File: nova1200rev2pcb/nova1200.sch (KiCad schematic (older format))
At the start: 190 parts, among them J1 Conn_02x26_Odd_Even, J2 Conn_02x05_Top_Bottom, J3 Conn_02x05_Top_Bottom, J4 Conn_02x01, J5 Conn_02x09_Odd_Even, J6 Conn_01x09, SW1 SW_SPST, SW10 SW_SPST, SW11 SW_SPST, SW12 SW_SPST, SW13 SW_SPST, SW14 SW_SPST, SW15 SW_SPST, SW16 SW_SPST, SW17 SW_SPDT_MSM, SW18 SW_SPDT_MSM, SW19 SW_SPDT_MSM, SW2 SW_SPST, SW20 SW_SPDT_MSM, SW21 SW_SPDT_MSM, SW22 SW_SPDT_MSM, SW23 SW_SPDT_MSM, SW24 SW_SPDT_MSM, SW25 SW_SPDT_MSM, SW26 SW_SPDT_MSM, SW3 SW_SPST, SW4 SW_SPST, SW5 SW_SPST, SW6 SW_SPST, SW7 SW_SPST, SW8 SW_SPST, SW9 SW_SPST, U1 74LS257, U10 74LS173, U11 74LS173, U12 74LS173, U13 74LS173, U14 74LS173, U15 74LS257, U16 74LS42, U17 74LS42, U18 74LS02, U19 74LS06, U2 74LS257, U20 74LS06, U21 74LS06, U3 74LS257, U4 74LS257, U5 74LS173, U6 74LS173, U7 74LS173, U8 74LS173, U9 74LS173

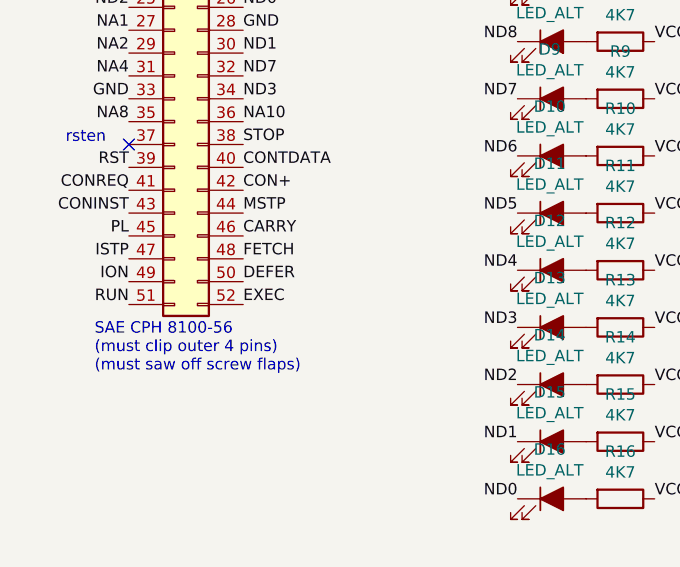
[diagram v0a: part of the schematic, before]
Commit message: Fixed error in pcb where EXEC and DEFER where swapped
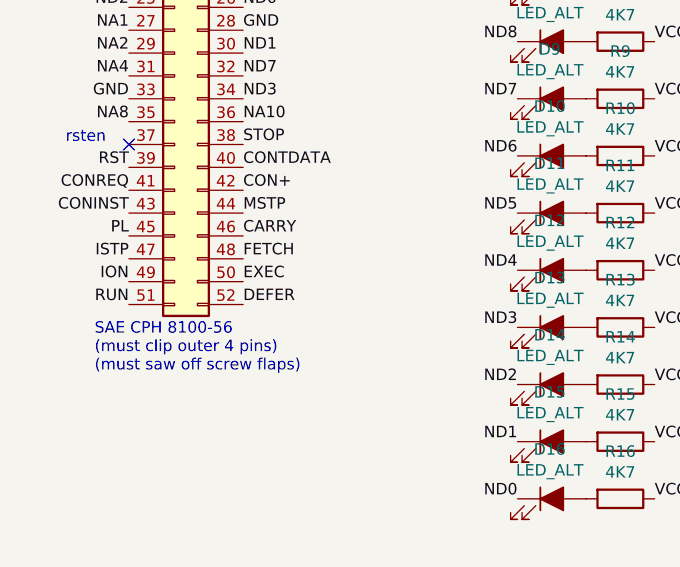
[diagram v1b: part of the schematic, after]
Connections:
- net DEFER: now also J1.52 (Pin_52); no longer J1.50 (Pin_50)
- net EXEC: now also J1.50 (Pin_50); no longer J1.52 (Pin_52)
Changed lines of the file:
@@
 Comment2 "Add pinheader for control switches"
 Comment3 "Idea: add extra register on SEL7"
-Comment4 ""
+Comment4 "Swapped EXEC and DEFER"
 $EndDescr
 $Comp
@@
 FETCH
 Text Label 1450 8900 0    50   ~ 0
+EXEC
+Text Label 1450 9000 0    50   ~ 0
 DEFER
-Text Label 1450 9000 0    50   ~ 0
-EXEC
 Text Notes 1500 7100 0    50   ~ 0
 vlamp

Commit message: Added jumper/resistor for Teensy application
// Nano to Teensy mapping:
//Arduino Teensy 3.5 Application
//GND	GND	GND
//D2	D0	D0
//..	..	..
//D12	D10	ENLCD1
//D13	A1	ENLCD2
//A0	A4	--- (KEYP)
//A1	A5	---
//A2	A6	LCD4
//A3	A7	LCD5
//A4	A8	LCD6
//A5	A9	LCD7
//A6	X (3.3 V)	---
//A7	--- (AGND)	---
//5V	Vin	5V
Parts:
- added R69: Jumper, Resistor_THT:R_Axial_DIN0204_L3.6mm_D1.6mm_P5.08mm_Horizontal, symbol Device:R_Small
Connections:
- net KEYL: now also R69.2
- net KEYP: now also R69.1
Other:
- note added: "A0"
- note added: "A0'"
- note added: "A1"
- note added: "A2"
- note added: "ENLCD1"
- note added: "ENLCD2"
- note added: "ERRORS: PINHEADERS WRONG FOOTPRINT\nAREF NOT CONNECTED TO KEYCHAIN; \nHole size Nova conn"
- note added: "FREE"
- note added: "I2C"
- note added: "I2C. LCD7"
- note added: "LCD4"
- note added: "LCD5"
- note added: "LCD6"
- note added: "Place when using Teensy 3.5 processor"
- note added: "Proposed to allow SPI"
- note added: "Proposed to isolate I2C \nfrom LCD"
- note added: "SPI"
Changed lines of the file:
@@
 Sheet 1 1
 Title "Computer controlled front panel for Nova 1200 computer"
-Date "2019-01-01"
+Date "2019-03-02"
 Rev "2"
 Comp "Marcel van Herk"
@@
 Comment2 "Add pinheader for control switches"
 Comment3 "Idea: add extra register on SEL7"
-Comment4 "Swapped EXEC and DEFER"
+Comment4 "Swapped EXEC and DEFER; added Teensy jumper"
 $EndDescr
 $Comp
@@
 Connection ~ 14800 8550
 Wire Wire Line
-	14400 8500 14600 8500
+	14400 8500 14450 8500
 Connection ~ 14600 8500
 Wire Wire Line
@@
 GND
 NoConn ~ 7650 7250
+Text Notes 12300 7100 0    50   ~ 0
+SPI
+Text Notes 12300 7200 0    50   ~ 0
+SPI
+Text Notes 12300 7300 0    50   ~ 0
+SPI
+Text Notes 12500 7000 0    50   ~ 0
+A0
+Text Notes 12500 7100 0    50   ~ 0
+A1
+Text Notes 12500 7200 0    50   ~ 0
+A2
+Text Notes 12500 7300 0    50   ~ 0
+A0'
+Text Notes 12450 6600 0    50   ~ 0
+ENLCD1
+Text Notes 12450 6700 0    50   ~ 0
+ENLCD2
+Text Notes 11800 6450 0    50   ~ 0
+Proposed to allow SPI
+Text Notes 14200 6700 0    50   ~ 0
+LCD4
+Text Notes 14200 6800 0    50   ~ 0
+LCD5
+Text Notes 14200 6900 0    50   ~ 0
+LCD6
+Text Notes 14200 7000 0    50   ~ 0
+I2C. LCD7
+Text Notes 14200 7100 0    50   ~ 0
+I2C
+Text Notes 14050 6450 0    50   ~ 0
+Proposed to isolate I2C \nfrom LCD
+Text Notes 14200 6600 0    50   ~ 0
+FREE
+Text Notes 14200 7300 0    50   ~ 0
+FREE
+Text Notes 14100 10250 0    50   ~ 0
+ERRORS: PINHEADERS WRONG FOOTPRINT\nAREF NOT CONNECTED TO KEYCHAIN; \nHole size Nova conn
+$Comp
+L Device:R_Small R69
+U 1 1 5C7B8356
+P 13350 9550
+F 0 "R69" V 13154 9550 50  0000 C CNN
+F 1 "Jumper" V 13245 9550 50  0000 C CNN
+F 2 "Resistor_THT:R_Axial_DIN0204_L3.6mm_D1.6mm_P5.08mm_Horizontal" H 13350 9550 50  0001 C CNN
+F 3 "~" H 13350 9550 50  0001 C CNN
+	1    13350 9550
+	0    1    1    0
+$EndComp
+Wire Wire Line
+	14450 8500 14450 9550
+Wire Wire Line
+	14450 9550 13450 9550
+Connection ~ 14450 8500
+Wire Wire Line
+	14450 8500 14600 8500
+Wire Wire Line
+	13250 9550 12600 9550
+Text Notes 12650 9700 0    50   ~ 0
+Place when using Teensy 3.5 processor
+Wire Wire Line
+	12600 9550 12600 8350
+Wire Wire Line
+	12600 8350 11800 8350
+Connection ~ 11800 8350
 $EndSCHEMATC
